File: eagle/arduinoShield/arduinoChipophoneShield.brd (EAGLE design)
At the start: 101.6 x 53.3 mm, 17 parts

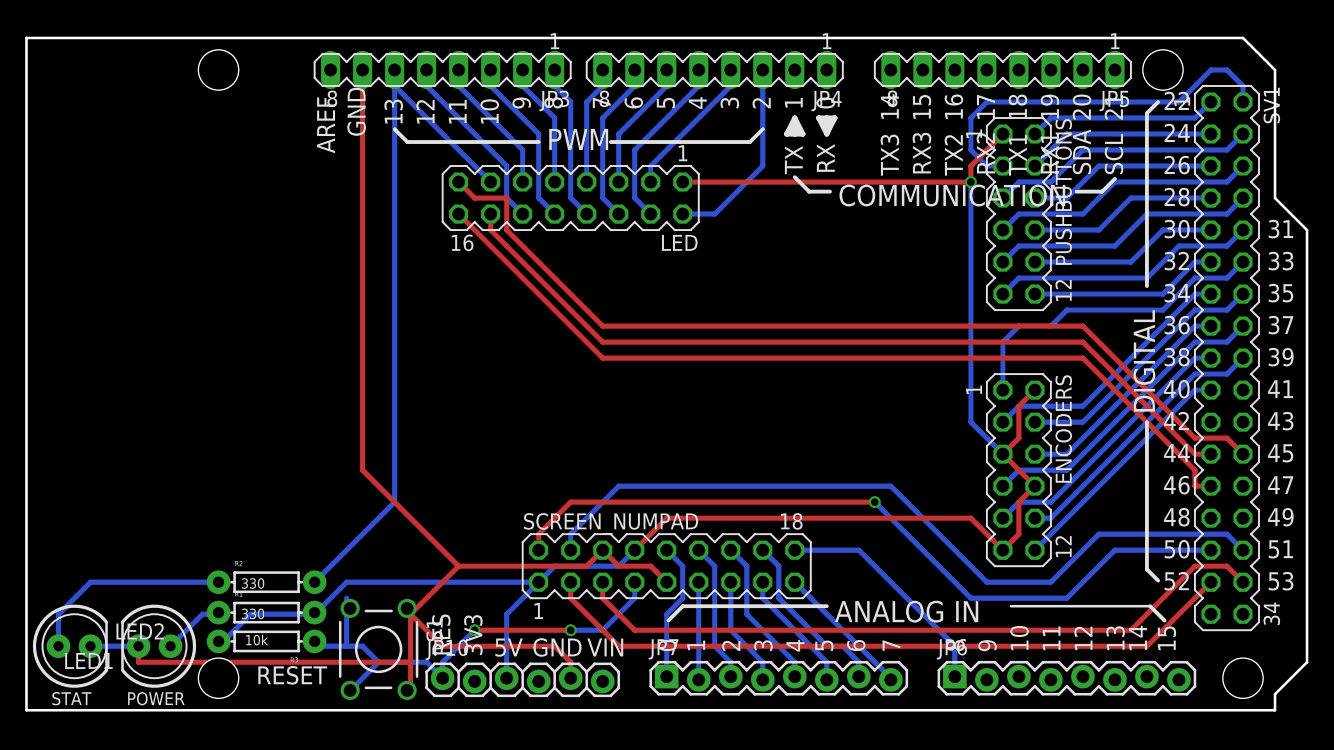
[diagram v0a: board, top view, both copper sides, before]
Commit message: Added MIDI I/O, took out status light
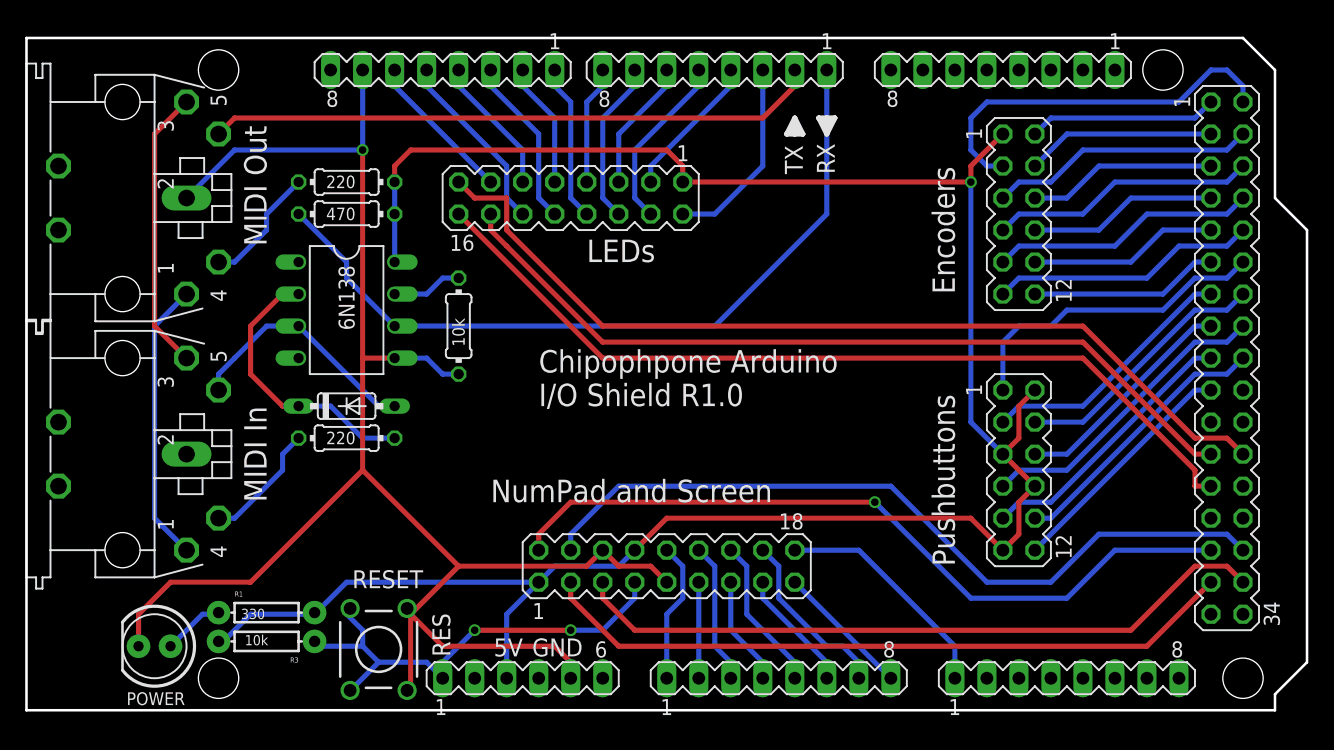
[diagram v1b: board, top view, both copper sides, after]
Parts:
- removed JP10: (no value), SparkFun:1X06_LOCK
- removed JP6, JP7: (no value), SparkFun:1X08_LOCK
- removed LED2: Green, SparkFun:LED5MM
- removed R2: 330, SparkFun:AXIAL-0.3
- added D1: 1N4148DO35-7, diode:DO35-7
- added JP1, JP2: (no value), con-lstb:MA08-1
- added MIDI_IN, MIDI_OUT: MAB5SH, con-hirschmann:MAB5SH
- added OK1: 6N138, optocoupler:DIL08
- added R4, R5: 220, rcl:0204/7
- added R6: 10k, rcl:0204/7
- added R7: 470, rcl:0204/7
- added SV2: (no value), con-lstb:MA06-1
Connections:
- removed net N$127: LED2.A, R2.P$1
- new net N$1: MIDI_IN.3, MIDI_OUT.3
- new net N$2: MIDI_IN.1, MIDI_OUT.1
- new net N$3: MIDI_OUT.4, R4.1
- new net N$5: D1.C, OK1.2, R5.2
- new net N$6: MIDI_IN.4, R5.1
- new net N$7: D1.A, MIDI_IN.5, OK1.3
- new net N$8: OK1.7, R6.2
- new net PE: MIDI_IN.PE, MIDI_IN.PE@, MIDI_OUT.PE, MIDI_OUT.PE@
- net 3.3: now also SV2.2; no longer JP10.2
- net 5V: now also OK1.8, R4.2, R7.2, SV2.3; no longer JP10.3
- net A0: now also JP1.1; no longer JP7.1
- net A1: now also JP1.2; no longer JP7.2
- net A10: now also JP2.3; no longer JP6.3
- net A11: now also JP2.4; no longer JP6.4
- net A12: now also JP2.5; no longer JP6.5
- net A13: now also JP2.6; no longer JP6.6
- net A14: now also JP2.7; no longer JP6.7
- net A15: now also JP2.8; no longer JP6.8
- net A2: now also JP1.3; no longer JP7.3
- net A3: now also JP1.4; no longer JP7.4
- net A4: now also JP1.5; no longer JP7.5
- net A5: now also JP1.6; no longer JP7.6
- net A6: now also JP1.7; no longer JP7.7
- net A7: now also JP1.8; no longer JP7.8
- net A8: now also JP2.1; no longer JP6.1
- net A9: now also JP2.2; no longer JP6.2
- net D13: no longer R2.P$2
- net GND: now also MIDI_OUT.2, OK1.5, R6.1, SV2.4, SV2.5; no longer JP10.4, JP10.5, LED2.K
- net RES: now also SV2.1; no longer JP10.1
- net RX0: now also OK1.6, R7.1
- net TX1: now also MIDI_OUT.5
- net VIN: now also SV2.6; no longer JP10.6
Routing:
- net RX0: track 0.00 -> 61.4 mm
- net TX1: track 0.00 -> 48.6 mm
- net D13: track 54.0 -> 12.0 mm
- net 5V: track 142.4 -> 175.2 mm
- net N$2: track 0.00 -> 22.4 mm
- net N$1: track 0.00 -> 22.4 mm
- net N$5: track 0.00 -> 22.2 mm
- net GND: track 114.6 -> 135.4 mm, vias 0 -> 1
- net N$7: track 0.00 -> 19.4 mm
- net N$127: track 16.3 -> 0.00 mm
- net N$6: track 0.00 -> 9.72 mm
- net N$3: track 0.00 -> 9.72 mm
- net N$8: track 0.00 -> 5.61 mm
- net RES: track 38.5 -> 36.5 mm
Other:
- board text added: "Chipophpone Arduino I/O Shield R1.0"
- board text added: "Encoders"
- board text added: "LEDs"
- board text added: "MIDI In"
- board text added: "MIDI Out"
- board text added: "NumPad and Screen"
- board text added: "Pushbuttons"
- board text removed: "0"
- board text removed: "1"
- board text removed: "10"
- board text removed: "11"
- board text removed: "12"
- board text removed: "13"
- board text removed: "14"
- board text removed: "15"
- board text removed: "16"
- board text removed: "17"
- board text removed: "18"
- board text removed: "19"
- board text removed: "2"
- board text removed: "20"
- board text removed: "21"
- board text removed: "22"
- board text removed: "24"
- board text removed: "26"
- board text removed: "28"
- board text removed: "3"
- board text removed: "30"
- board text removed: "31"
- board text removed: "32"
- board text removed: "33"
- board text removed: "34"
- board text removed: "35"
- board text removed: "36"
- board text removed: "37"
- board text removed: "38"
- board text removed: "39"
- board text removed: "3V3"
- board text removed: "4"
- board text removed: "40"
- board text removed: "41"
- board text removed: "42"
- board text removed: "43"
- board text removed: "44"
- board text removed: "45"
- board text removed: "46"
- board text removed: "47"
- board text removed: "48"
- board text removed: "49"
- board text removed: "5"
- board text removed: "50"
- board text removed: "51"
- board text removed: "52"
- board text removed: "53"
- board text removed: "6"
- board text removed: "7"
- board text removed: "8"
- board text removed: "9"
- board text removed: "ANALOG IN"
- board text removed: "AREF"
- board text removed: "COMMUNICATION"
- board text removed: "DIGITAL"
- board text removed: "PWM"
- board text removed: "RX1"
- board text removed: "RX2"
- board text removed: "RX3"
- board text removed: "SCL"
- board text removed: "SDA"
- board text removed: "STAT"
- board text removed: "TX1"
- board text removed: "TX2"
- board text removed: "TX3"
- board text removed: "VIN"

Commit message: Added ground/power plane as well as 5V DIN forwarding switches on Arduino Board
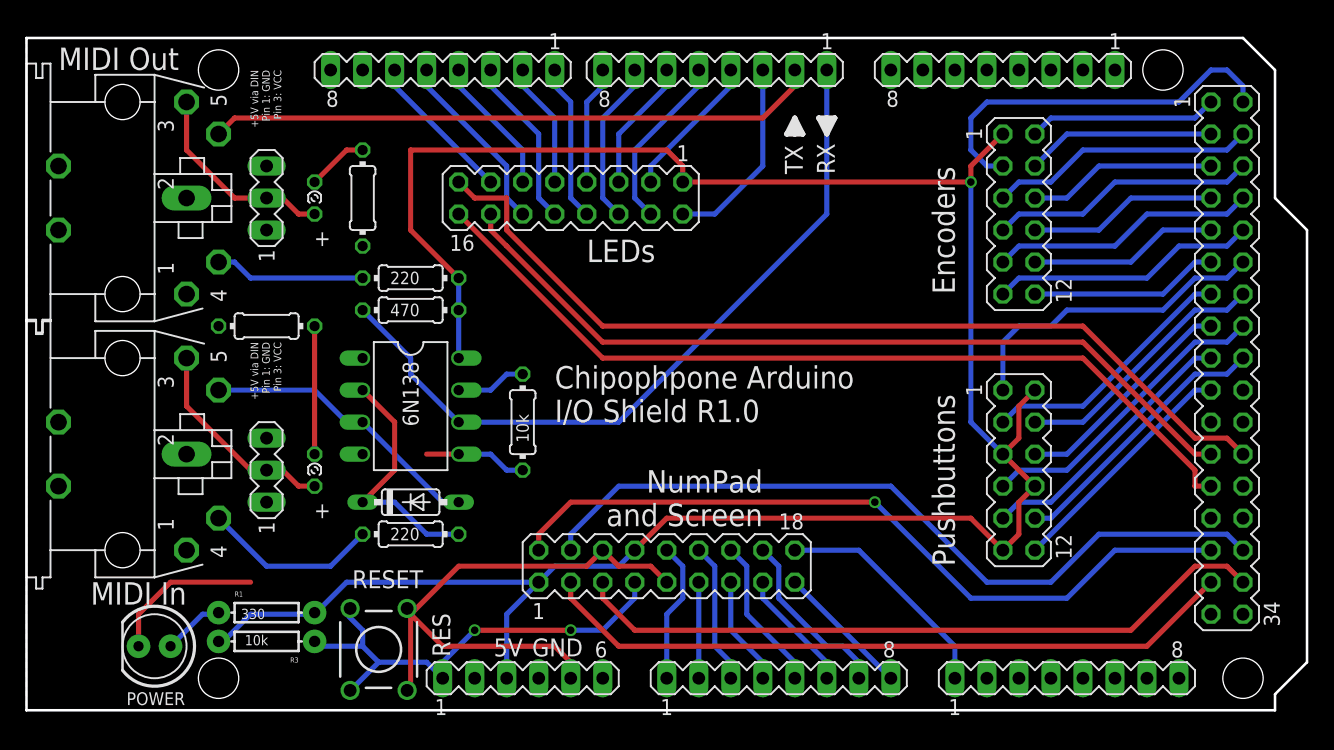
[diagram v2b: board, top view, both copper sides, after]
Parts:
- added LED2, LED3: (no value), led:LSU260
- added R2, R8: 4k7, resistor:0204/7
- added SV3, SV4: (no value), con-lstb:MA03-1
- moved OK1 9.16 mm to (30.5, 24.1)
- moved R5 9.16 mm to (30.5, 14.0)
- moved D1 9.16 mm to (30.5, 16.5)
- moved R4 9.16 mm to (30.5, 34.3)
- moved R6 9.16 mm to (39.4, 22.9)
- moved R7 9.16 mm to (30.5, 31.8)
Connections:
- removed net PE: MIDI_IN.PE, MIDI_IN.PE@, MIDI_OUT.PE, MIDI_OUT.PE@
- new net N$13: LED3.K, R8.2
- new net N$4: LED2.K, R2.2
- net 5V: now also SV3.1, SV4.1
- net GND: now also MIDI_IN.1, MIDI_IN.PE, MIDI_IN.PE@, MIDI_OUT.1, MIDI_OUT.PE, MIDI_OUT.PE@, R2.1, R8.1, SV3.3, SV4.3
- net N$1: now also LED3.A, SV4.2; no longer MIDI_OUT.3
- net N$2: now also LED2.A, MIDI_OUT.3, SV3.2; no longer MIDI_IN.1, MIDI_OUT.1
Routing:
- net GND: track 135.4 -> 64.7 mm, vias 1 -> 0
- net N$13: track 0.00 -> 10.2 mm
- net 5V: track 175.2 -> 183.9 mm
- net N$2: track 22.4 -> 16.1 mm
- net N$1: track 22.4 -> 16.6 mm
- net N$4: track 0.00 -> 4.86 mm
- net N$6: track 9.72 -> 14.1 mm
- net N$7: track 19.4 -> 22.7 mm
- net N$5: track 22.2 -> 19.7 mm
- net N$3: track 9.72 -> 12.0 mm
- net RX0: track 61.4 -> 59.5 mm
- added copper zone on layer 16, net 5V
- added copper zone on layer 1, net GND
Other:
- board text added: "+"
- board text added: "+5V via DIN Pin 1: GND Pin 3: VCC"
